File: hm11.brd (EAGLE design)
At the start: 17.1 x 24.4 mm, 2 parts

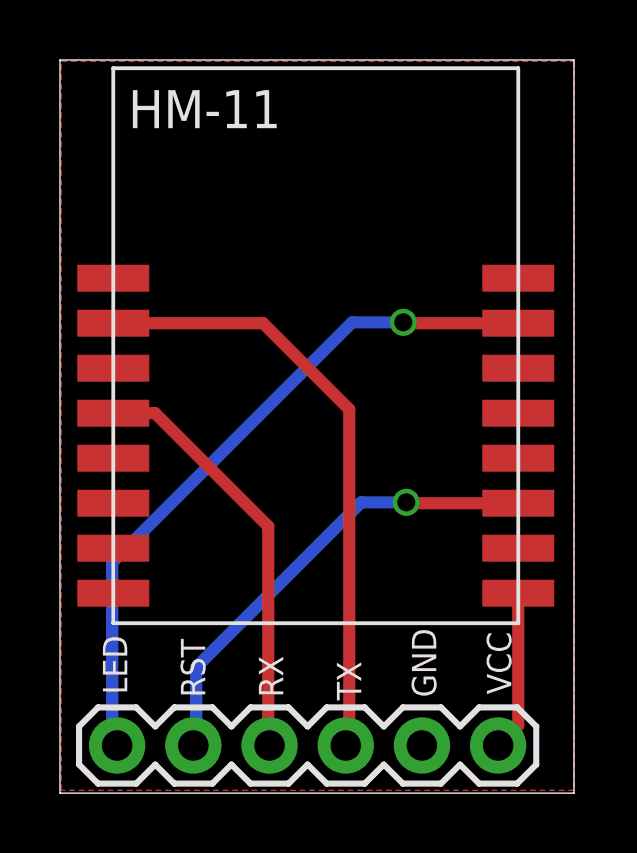
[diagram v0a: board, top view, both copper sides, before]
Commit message: Reduced size of board, cleaned up connections
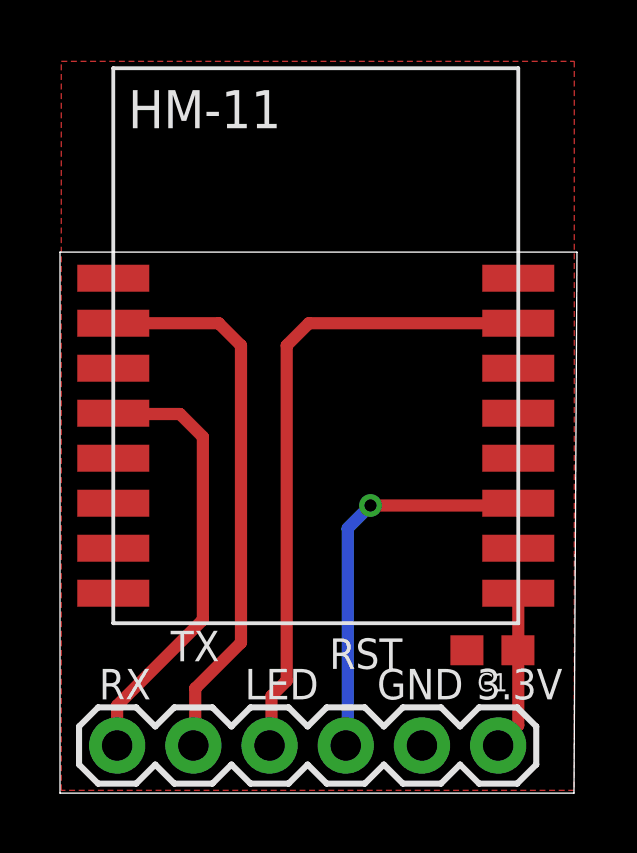
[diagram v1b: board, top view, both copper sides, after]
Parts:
- added C1: 1.0uF, SparkFun-Capacitors:0603
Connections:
- net GND: now also C1.2
- net N$2: now also C1.1
- net N$3: now also JP1.5; no longer JP1.3
- net N$4: now also JP1.4; no longer JP1.6
- net N$5: now also JP1.6; no longer JP1.4
- net N$6: now also JP1.3; no longer JP1.5
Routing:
- net N$6: track 15.7 -> 13.3 mm
- net N$3: track 20.3 -> 18.6 mm
- net N$4: track 23.0 -> 21.6 mm, vias 1 -> 0
- net N$5: track 14.1 -> 14.8 mm
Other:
- board size 17.1 x 24.4 mm -> 17.2 x 18 mm
- board text added: "3.3V"
- board text added: "WestSideElectronics JDY-08/HM-11 BLE Breakout Board"
- board text removed: "HM-11 breakout board"
- board text removed: "RESET"
- board text removed: "VCC"
- board text removed: "platis.solutions"

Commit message: update traces
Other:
- board size 17.2 x 18 mm -> 17 x 18 mm
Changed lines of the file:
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@@
 <layer number="23" name="tOrigins" color="15" fill="1" visible="yes" active="yes"/>
 <layer number="24" name="bOrigins" color="15" fill="1" visible="yes" active="yes"/>
-<layer number="25" name="tNames" color="7" fill="1" visible="no" active="yes"/>
-<layer number="26" name="bNames" color="7" fill="1" visible="no" active="yes"/>
-<layer number="27" name="tValues" color="7" fill="1" visible="no" active="yes"/>
-<layer number="28" name="bValues" color="7" fill="1" visible="no" active="yes"/>
-<layer number="29" name="tStop" color="7" fill="3" visible="yes" active="yes"/>
-<layer number="30" name="bStop" color="7" fill="6" visible="yes" active="yes"/>
+<layer number="25" name="tNames" color="7" fill="1" visible="yes" active="yes"/>
+<layer number="26" name="bNames" color="7" fill="1" visible="yes" active="yes"/>
+<layer number="27" name="tValues" color="7" fill="1" visible="yes" active="yes"/>
+<layer number="28" name="bValues" color="7" fill="1" visible="yes" active="yes"/>
+<layer number="29" name="tStop" color="7" fill="3" visible="no" active="yes"/>
+<layer number="30" name="bStop" color="7" fill="6" visible="no" active="yes"/>
 <layer number="31" name="tCream" color="7" fill="4" visible="no" active="yes"/>
 <layer number="32" name="bCream" color="7" fill="5" visible="no" active="yes"/>
@@
 <board>
 <plain>
-<wire x1="28.2575" y1="21.9075" x2="45.39" y2="21.9075" width="0" layer="20"/>
-<wire x1="45.39" y1="21.9075" x2="45.49" y2="39.9415" width="0" layer="20"/>
-<wire x1="45.49" y1="39.9415" x2="28.2575" y2="39.9415" width="0" layer="20"/>
+<wire x1="28.2575" y1="21.9075" x2="45.2755" y2="21.9075" width="0" layer="20"/>
+<wire x1="45.2755" y1="21.9075" x2="45.2755" y2="39.9415" width="0" layer="20"/>
+<wire x1="45.2755" y1="39.9415" x2="28.2575" y2="39.9415" width="0" layer="20"/>
 <wire x1="28.2575" y1="39.9415" x2="28.2575" y2="21.9075" width="0" layer="20"/>
 <text x="31.288" y="26.048" size="1.016" layer="21" font="vector" ratio="15" rot="R180">RX</text>
@@
 <attribute name="VALUE" x="44.1325" y="26.67" size="1.27" layer="27" rot="R180"/>
 </element>
-<element name="C1" library="SparkFun-Capacitors" package="0603" value="1.0uF" x="42.672" y="26.67" rot="R180">
+<element name="C1" library="SparkFun-Capacitors" package="0603" value="1.0uF" x="42.672" y="26.67" smashed="yes" rot="R180">
 <attribute name="PROD_ID" value="CAP-00868" x="42.672" y="26.67" size="1.778" layer="27" font="vector" ratio="15" rot="R180" display="off"/>
+<attribute name="VALUE" x="42.672" y="27.432" size="0.6096" layer="27" font="vector" ratio="20" rot="R180" align="top-center"/>
 </element>
 </elements>

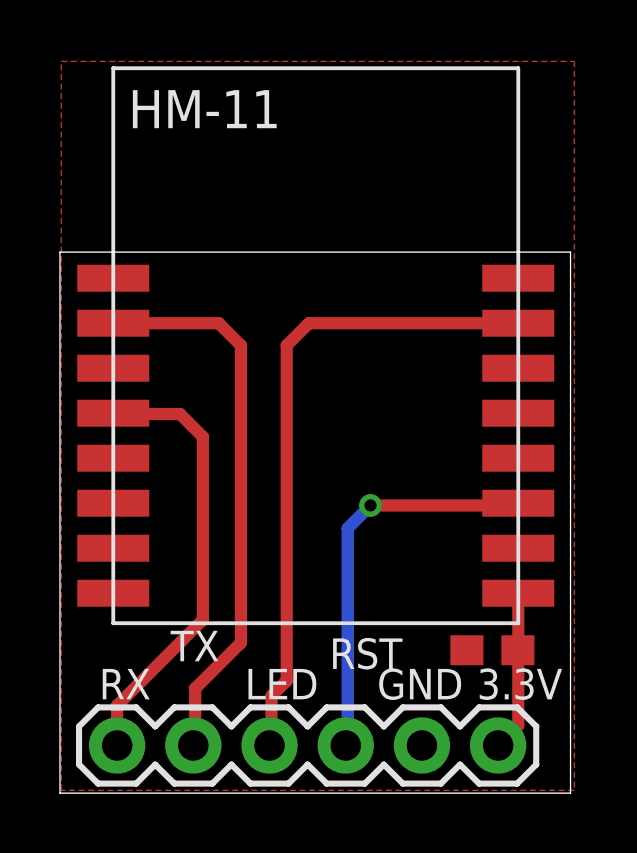
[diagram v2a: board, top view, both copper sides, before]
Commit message: Updated pin locations
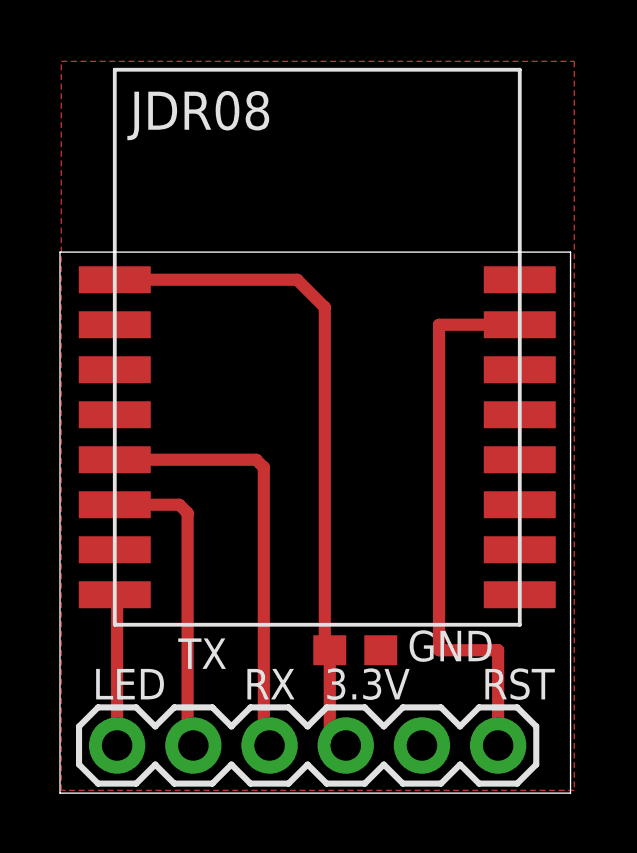
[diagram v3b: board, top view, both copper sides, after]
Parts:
- removed U$1: HM-11, hm-11:HM-11
- added U$2: JDR08, hm-11:JDC08
- moved C1 4.57 mm to (38.1, 26.7)
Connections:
- removed net N$4: JP1.4, U$1.PIO1
- removed net N$6: JP1.3, U$1.RESETB
- new net N$7: JP1.6, U$2.LED
- new net N$8: C1.2, JP1.3, U$2.VCC
- net GND: now also C1.1, U$2.GND; no longer C1.2, U$1.GND
- net N$2: now also U$2.RESET; no longer C1.1, U$1.VCC
- net N$3: now also U$2.TX; no longer U$1.UART_TX
- net N$5: now also JP1.4, U$2.RX; no longer JP1.6, U$1.UART_RX
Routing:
- net N$8: track 0.00 -> 22.3 mm
- net N$4: track 21.6 -> 0.00 mm
- net N$2: track 5.36 -> 18.7 mm
- net N$6: track 13.3 -> 0.00 mm, vias 1 -> 0
- net N$3: track 18.6 -> 10.4 mm
- net N$7: track 0.00 -> 5.06 mm
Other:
- board text added: "WestSideElectronics JDY-08 BLE Breakout Board"
- board text removed: "WestSideElectronics JDY-08/HM-11 BLE Breakout Board"
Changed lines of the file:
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@@
 <wire x1="45.2755" y1="39.9415" x2="28.2575" y2="39.9415" width="0" layer="20"/>
 <wire x1="28.2575" y1="39.9415" x2="28.2575" y2="21.9075" width="0" layer="20"/>
-<text x="31.288" y="26.048" size="1.016" layer="21" font="vector" ratio="15" rot="R180">RX</text>
-<text x="33.574" y="27.318" size="1.016" layer="21" font="vector" ratio="15" rot="R180">TX</text>
-<text x="36.876" y="26.048" size="1.016" layer="21" font="vector" ratio="15" rot="R180">LED</text>
-<text x="39.67" y="27.064" size="1.016" layer="21" font="vector" ratio="15" rot="R180">RST</text>
-<text x="41.702" y="26.048" size="1.016" layer="21" font="vector" ratio="15" rot="R180">GND</text>
-<text x="45.004" y="26.048" size="1.016" layer="21" font="vector" ratio="15" rot="R180">3.3V</text>
+<text x="36.114" y="26.048" size="1.016" layer="21" font="vector" ratio="15" rot="R180">RX</text>
+<text x="33.828" y="27.064" size="1.016" layer="21" font="vector" ratio="15" rot="R180">TX</text>
+<text x="31.796" y="26.048" size="1.016" layer="21" font="vector" ratio="15" rot="R180">LED</text>
+<text x="44.75" y="26.048" size="1.016" layer="21" font="vector" ratio="15" rot="R180">RST</text>
+<text x="42.718" y="27.318" size="1.016" layer="21" font="vector" ratio="15" rot="R180">GND</text>
+<text x="39.924" y="26.048" size="1.016" layer="21" font="vector" ratio="15" rot="R180">3.3V</text>
 <text x="42.926" y="33.528" size="0.8128" layer="22" font="vector" ratio="15" rot="MR0">WestSideElectronics
-JDY-08/HM-11 BLE
+JDY-08 BLE
 Breakout Board</text>
-<text x="41.102" y="27.318" size="1.016" layer="22" font="vector" ratio="15" rot="MR180">3.3V</text>
-<text x="38.816" y="26.048" size="1.016" layer="22" font="vector" ratio="15" rot="MR180">GND</text>
-<text x="36.276" y="27.318" size="1.016" layer="22" font="vector" ratio="15" rot="MR180">RST</text>
-<text x="33.99" y="26.048" size="1.016" layer="22" font="vector" ratio="15" rot="MR180">LED</text>
+<text x="36.53" y="26.048" size="1.016" layer="22" font="vector" ratio="15" rot="MR180">3.3V</text>
+<text x="39.832" y="27.318" size="1.016" layer="22" font="vector" ratio="15" rot="MR180">GND</text>
+<text x="41.864" y="26.048" size="1.016" layer="22" font="vector" ratio="15" rot="MR180">RST</text>
+<text x="28.91" y="26.048" size="1.016" layer="22" font="vector" ratio="15" rot="MR180">LED</text>
 <text x="31.958" y="27.064" size="1.016" layer="22" font="vector" ratio="15" rot="MR180">TX</text>
-<text x="29.164" y="26.048" size="1.016" layer="22" font="vector" ratio="15" rot="MR180">RX</text>
+<text x="34.244" y="26.048" size="1.016" layer="22" font="vector" ratio="15" rot="MR180">RX</text>
 <wire x1="29.972" y1="37.338" x2="43.434" y2="37.338" width="0.254" layer="22"/>
 <wire x1="43.434" y1="37.338" x2="43.942" y2="36.83" width="0.254" layer="22"/>
@@
 </autorouter>
 <elements>
-<element name="U$1" library="hm-11" package="HM-11" value="HM-11" x="37.0332" y="33.0708"/>
 <element name="JP1" library="SparkFun-Connectors" package="1X06" value="" x="42.8625" y="23.495" smashed="yes" rot="R180">
 <attribute name="VALUE" x="44.1325" y="26.67" size="1.27" layer="27" rot="R180"/>
 </element>
-<element name="C1" library="SparkFun-Capacitors" package="0603" value="1.0uF" x="42.672" y="26.67" smashed="yes" rot="R180">
-<attribute name="PROD_ID" value="CAP-00868" x="42.672" y="26.67" size="1.778" layer="27" font="vector" ratio="15" rot="R180" display="off"/>
-<attribute name="VALUE" x="42.672" y="27.432" size="0.6096" layer="27" font="vector" ratio="20" rot="R180" align="top-center"/>
+<element name="C1" library="SparkFun-Capacitors" package="0603" value="1.0uF" x="38.1" y="26.67" smashed="yes" rot="R180">
+<attribute name="PROD_ID" value="CAP-00868" x="38.1" y="26.67" size="1.778" layer="27" font="vector" ratio="15" rot="R180" display="off"/>
+<attribute name="VALUE" x="38.1" y="27.432" size="0.6096" layer="27" font="vector" ratio="20" rot="R180" align="top-center"/>
 </element>
+<element name="U$2" library="hm-11" package="JDC08" value="JDR08" x="37.084" y="35.56"/>
 </elements>
 <signals>
 <signal name="N$1">
 </signal>
-<signal name="N$4">
-<contactref element="U$1" pad="PIO1"/>
-<contactref element="JP1" pad="4"/>
-<wire x1="43.5332" y1="37.5708" x2="36.5548" y2="37.5708" width="0.4064" layer="1"/>
-<wire x1="36.5548" y1="37.5708" x2="35.814" y2="36.83" width="0.4064" layer="1"/>
-<wire x1="35.814" y1="36.83" x2="35.814" y2="25.654" width="0.4064" layer="1"/>
-<wire x1="35.814" y1="25.654" x2="35.306" y2="25.146" width="0.4064" layer="1"/>
-<wire x1="35.306" y1="25.146" x2="35.306" y2="23.5585" width="0.4064" layer="1"/>
-<wire x1="35.306" y1="23.5585" x2="35.2425" y2="23.495" width="0.4064" layer="1"/>
-</signal>
 <signal name="N$2">
-<contactref element="U$1" pad="VCC"/>
 <contactref element="JP1" pad="1"/>
-<wire x1="43.5332" y1="28.5708" x2="43.5332" y2="26.67" width="0.4064" layer="1"/>
-<wire x1="43.5332" y1="26.67" x2="43.5332" y2="24.1657" width="0.4064" layer="1"/>
-<wire x1="43.5332" y1="24.1657" x2="42.8625" y2="23.495" width="0.4064" layer="1"/>
-<contactref element="C1" pad="1"/>
-<wire x1="43.522" y1="26.67" x2="43.5332" y2="26.67" width="0.4064" layer="1"/>
-</signal>
-<signal name="N$6">
-<contactref element="U$1" pad="RESETB"/>
-<contactref element="JP1" pad="3"/>
-<wire x1="38.608" y1="31.496" x2="43.4584" y2="31.496" width="0.4064" layer="1"/>
-<wire x1="43.4584" y1="31.496" x2="43.5332" y2="31.5708" width="0.4064" layer="1"/>
-<via x="38.608" y="31.496" extent="1-16" drill="0.4064"/>
-<wire x1="38.608" y1="31.496" x2="37.846" y2="30.734" width="0.4064" layer="16"/>
-<wire x1="37.846" y1="30.734" x2="37.846" y2="23.5585" width="0.4064" layer="16"/>
-<wire x1="37.846" y1="23.5585" x2="37.7825" y2="23.495" width="0.4064" layer="16"/>
+<contactref element="U$2" pad="RESET"/>
+<wire x1="42.8625" y1="23.495" x2="42.8625" y2="26.67" width="0.4064" layer="1"/>
+<wire x1="42.8625" y1="26.67" x2="40.894" y2="26.67" width="0.4064" layer="1"/>
+<wire x1="40.894" y1="26.67" x2="40.894" y2="37.52" width="0.4064" layer="1"/>
+<wire x1="40.894" y1="37.52" x2="43.584" y2="37.52" width="0.4064" layer="1"/>
 </signal>
 <signal name="GND">
-<contactref element="U$1" pad="GND"/>
 <contactref element="JP1" pad="2"/>
 <polygon width="0.4064" layer="1">
@@
 <vertex x="28.3" y="22"/>
 </polygon>
+<contactref element="U$2" pad="GND"/>
+<contactref element="C1" pad="1"/>
+</signal>
+<signal name="N$3">
+<contactref element="U$2" pad="TX"/>
+<contactref element="JP1" pad="5"/>
+<wire x1="32.7025" y1="23.495" x2="32.512" y2="23.6855" width="0.4064" layer="1"/>
+<wire x1="32.512" y1="23.6855" x2="32.512" y2="31.242" width="0.4064" layer="1"/>
+<wire x1="32.512" y1="31.242" x2="32.234" y2="31.52" width="0.4064" layer="1"/>
+<wire x1="32.234" y1="31.52" x2="30.084" y2="31.52" width="0.4064" layer="1"/>
+</signal>
+<signal name="N$5">
+<contactref element="U$2" pad="RX"/>
+<contactref element="JP1" pad="4"/>
+<wire x1="35.2425" y1="23.495" x2="35.052" y2="23.6855" width="0.4064" layer="1"/>
+<wire x1="35.052" y1="23.6855" x2="35.052" y2="32.766" width="0.4064" layer="1"/>
+<wire x1="35.052" y1="32.766" x2="34.798" y2="33.02" width="0.4064" layer="1"/>
+<wire x1="34.798" y1="33.02" x2="30.084" y2="33.02" width="0.4064" layer="1"/>
+</signal>
+<signal name="N$7">
+<contactref element="U$2" pad="LED"/>
+<contactref element="JP1" pad="6"/>
+<wire x1="30.084" y1="28.52" x2="30.1625" y2="28.4415" width="0.4064" layer="1"/>
+<wire x1="30.1625" y1="28.4415" x2="30.1625" y2="23.495" width="0.4064" layer="1"/>
+</signal>
+<signal name="N$8">
 <contactref element="C1" pad="2"/>
-</signal>
-<signal name="N$3">
-<contactref element="U$1" pad="UART_TX"/>
-<contactref element="JP1" pad="5"/>
-<wire x1="30.0332" y1="37.5708" x2="33.5492" y2="37.5708" width="0.4064" layer="1"/>
-<wire x1="33.5492" y1="37.5708" x2="34.29" y2="36.83" width="0.4064" layer="1"/>
-<wire x1="34.29" y1="36.83" x2="34.29" y2="26.924" width="0.4064" layer="1"/>
-<wire x1="34.29" y1="26.924" x2="32.766" y2="25.4" width="0.4064" layer="1"/>
-<wire x1="32.766" y1="25.4" x2="32.766" y2="23.5585" width="0.4064" layer="1"/>
-<wire x1="32.766" y1="23.5585" x2="32.7025" y2="23.495" width="0.4064" layer="1"/>
-</signal>
-<signal name="N$5">
-<contactref element="U$1" pad="UART_RX"/>
-<contactref element="JP1" pad="6"/>
-<wire x1="30.1625" y1="23.495" x2="30.1625" y2="24.8285" width="0.4064" layer="1"/>
-<wire x1="30.1625" y1="24.8285" x2="33.02" y2="27.686" width="0.4064" layer="1"/>
-<wire x1="33.02" y1="27.686" x2="33.02" y2="33.782" width="0.4064" layer="1"/>
-<wire x1="33.02" y1="33.782" x2="32.258" y2="34.544" width="0.4064" layer="1"/>
-<wire x1="32.258" y1="34.544" x2="30.06" y2="34.544" width="0.4064" layer="1"/>
-<wire x1="30.06" y1="34.544" x2="30.0332" y2="34.5708" width="0.4064" layer="1"/>
+<contactref element="JP1" pad="3"/>
+<contactref element="U$2" pad="VCC"/>
+<wire x1="37.7825" y1="23.495" x2="37.25" y2="24.0275" width="0.4064" layer="1" curve="-90"/>
+<wire x1="37.25" y1="24.0275" x2="37.25" y2="26.67" width="0.4064" layer="1"/>
+<wire x1="37.25" y1="26.67" x2="37.084" y2="26.836" width="0.4064" layer="1" curve="-90"/>
+<wire x1="37.084" y1="26.836" x2="37.084" y2="38.1" width="0.4064" layer="1"/>
+<wire x1="37.084" y1="38.1" x2="36.164" y2="39.02" width="0.4064" layer="1"/>
+<wire x1="36.164" y1="39.02" x2="30.084" y2="39.02" width="0.4064" layer="1"/>
 </signal>
 </signals>
